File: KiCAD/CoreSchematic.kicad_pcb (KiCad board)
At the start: 2 copper layers, 97.4 x 71 mm, 47 parts, among them J101 Conn_01x06_Female, J201 USB_B_Micro, Q201 Q_NPN_BEC, Q202 Q_NPN_BEC, SW101 SW_Push, SW102 SW_Push, SW103 SW_Push, U201 FT231XQ, U301 AP2114H-3_3TRG1, U302 BQ27441-G1

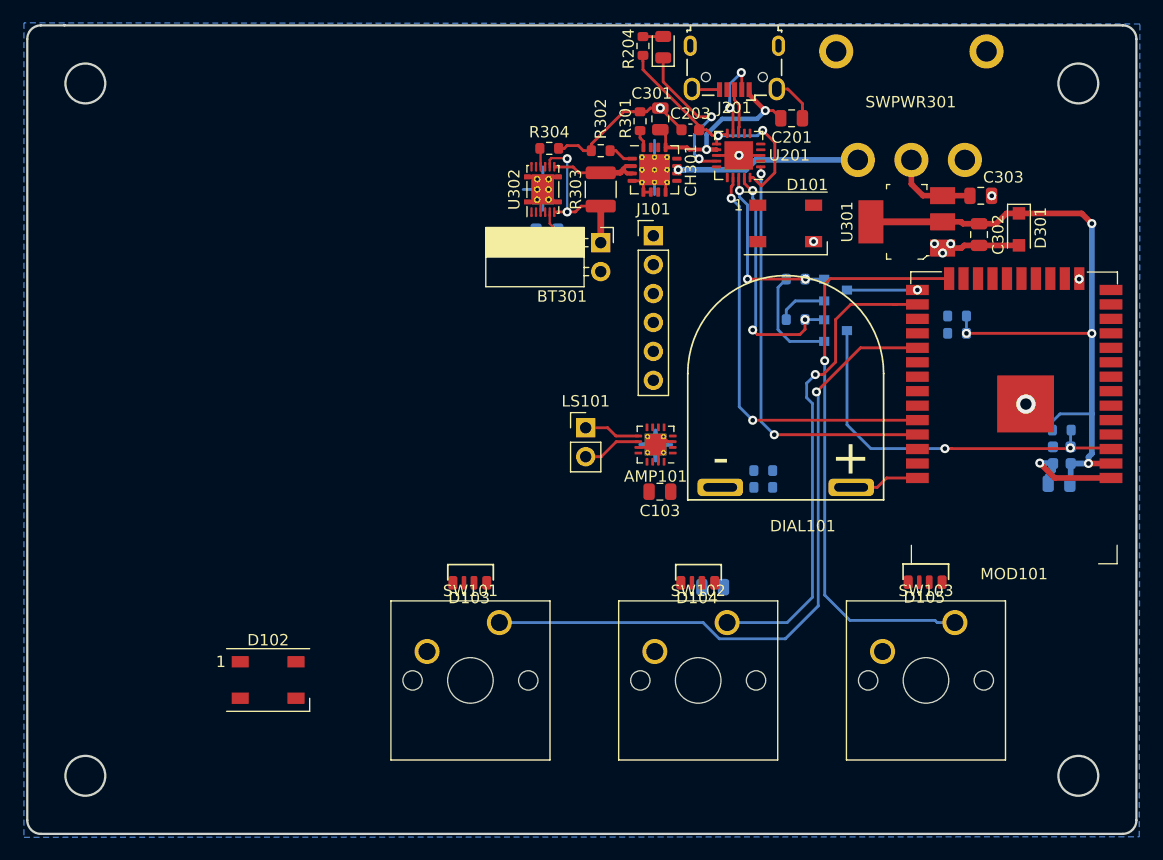
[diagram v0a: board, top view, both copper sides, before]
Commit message: Add gitmodules and extend KiCAD schematics
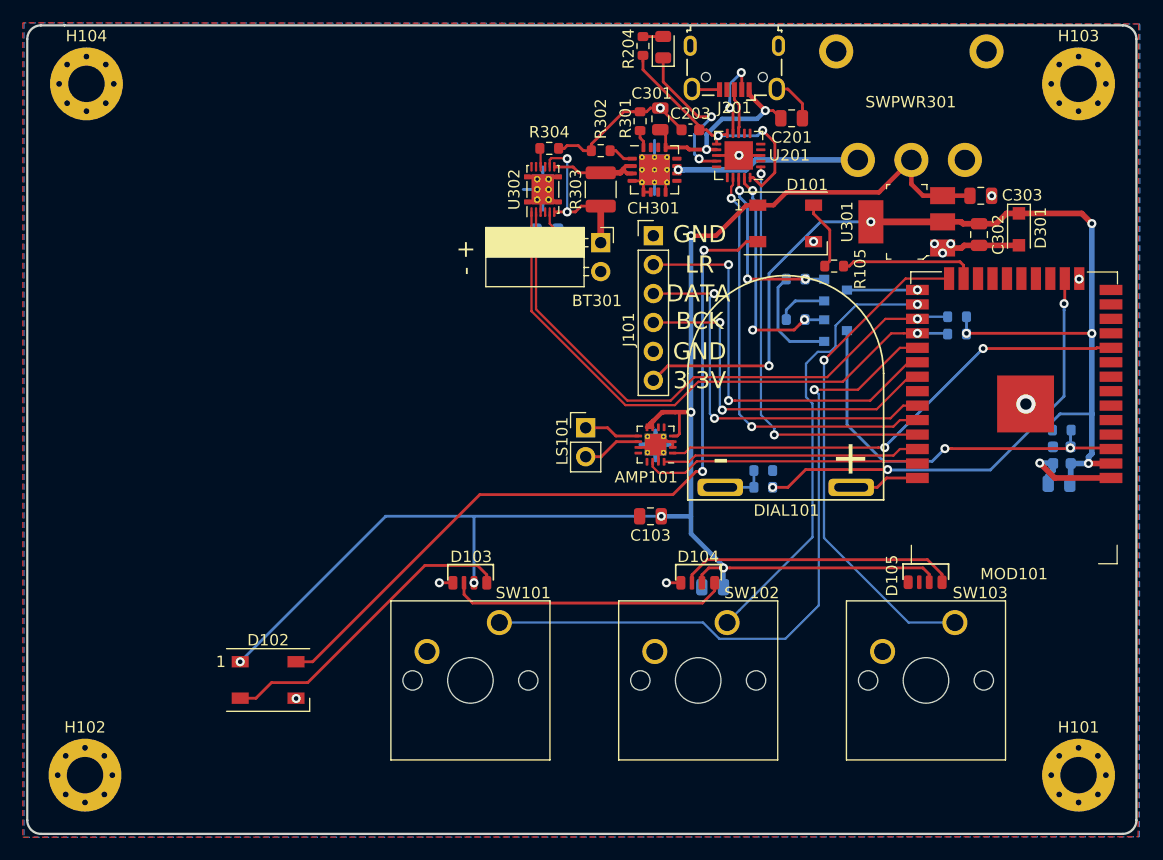
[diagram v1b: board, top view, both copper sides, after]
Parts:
- added H101: MountingHole_Pad, MountingHole:MountingHole_3.2mm_M3_Pad_Via, F.Cu at (184.7, 120.0)
- added H102: MountingHole_Pad, MountingHole:MountingHole_3.2mm_M3_Pad_Via, F.Cu at (97.4, 120.0)
- added H103: MountingHole_Pad, MountingHole:MountingHole_3.2mm_M3_Pad_Via, F.Cu at (184.7, 59.3)
- added H104: MountingHole_Pad, MountingHole:MountingHole_3.2mm_M3_Pad_Via, F.Cu at (97.5, 59.3)
- added R105: 10k, Resistor_SMD:R_0603_1608Metric, F.Cu at (163.2, 75.3)
- added SYM101: SYM_Earth_Protective_Small, XasPrints:DragonIcon_25mm, B.Cu at (116.6, 71.9)
- CH301: value BQ24323 -> BQ24232
- moved C103 2.31 mm to (147.1, 97.3)
- moved R103 1.59 mm to (174.0, 81.3)
- moved R104 1.46 mm to (174.0, 79.8)
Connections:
- AMP101 pad 2: Net-(AMP101-Pad2) -> GND
- AMP101 pad 4: Net-(AMP101-Pad4) -> +BATT
- D101 pad 1: +3V3 -> +BATT
- D101 pad 2: Net-(D101-Pad2) -> /BTN_LEDS
- D105 pad 2: /SPEAKER_LED -> Net-(D105-Pad2)
- MOD101 pad 16: Net-(MOD101-Pad16) -> /DIAL_PWM
- MOD101 pad 23: /BTN_LEDS -> Net-(MOD101-Pad23)
- MOD101 pad 27: SDA -> SCL
- MOD101 pad 28: SCL -> SDA
- MOD101 pad 36: /OUT_LR -> /OUT_BCK
- MOD101 pad 37: /OUT_BCK -> /OUT_LR
- R101 pad 1: Net-(R101-Pad1) -> /DIAL_PWM
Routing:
- net +BATT: track 7.69 -> 143.0 mm, vias 0 -> 6
- net /BTN_LEDS: track 0.00 -> 67.1 mm, vias 0 -> 2
- net SDA: track 0.00 -> 51.3 mm, vias 0 -> 1
- net SCL: track 0.00 -> 51.1 mm, vias 0 -> 1
- net /OUT_DATA: track 0.00 -> 42.3 mm, vias 0 -> 2
- net /DIAL_PWM: track 0.00 -> 39.3 mm, vias 0 -> 3
- net /MIC_LR: track 0.00 -> 36.5 mm, vias 0 -> 2
- net /MIC_DATA: track 0.00 -> 34.9 mm, vias 0 -> 2
- net /MIC_BCK: track 0.00 -> 32.0 mm, vias 0 -> 2
- net +3V3: track 64.0 -> 93.6 mm, vias 4 -> 6
- net Net-(D102-Pad2): track 0.00 -> 27.5 mm
- net Net-(D103-Pad2): track 0.00 -> 24.5 mm
- net Net-(D104-Pad2): track 0.00 -> 24.4 mm
- net /OUT_LR: track 0.00 -> 24.4 mm
- net /OUT_BCK: track 0.00 -> 22.7 mm
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- added copper zone on F.Cu, net GND
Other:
- outline, holes or cut-outs redrawn
- board text added: "- +"
- board text added: "3.3V"
- board text added: "BCK"
- board text added: "DATA"
- board text added: "GND"
- board text added: "LR"
- board text added: "Made with love for Wuff <3 Merry christmas 2020! - Xasin, Neira and Mesh"
